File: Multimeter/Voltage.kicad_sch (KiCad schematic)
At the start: 9 parts, among them U2 LM358, U3 CD4007

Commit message: Renamed from Project1 to Multimeter
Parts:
- U3: symbol Project1:CD4007 -> Multimeter:CD4007
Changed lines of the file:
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@@
     (pin "8")
   )
-  (symbol (lib_id "Project1:CD4007") (at 158.75 78.74 0) (unit 1)
+  (symbol (lib_id "Multimeter:CD4007") (at 158.75 78.74 0) (unit 1)
     (in_bom yes) (on_board yes) (fields_autoplaced)
     (property "Reference" "U3" (id 0) (at 158.75 63.4705 0))

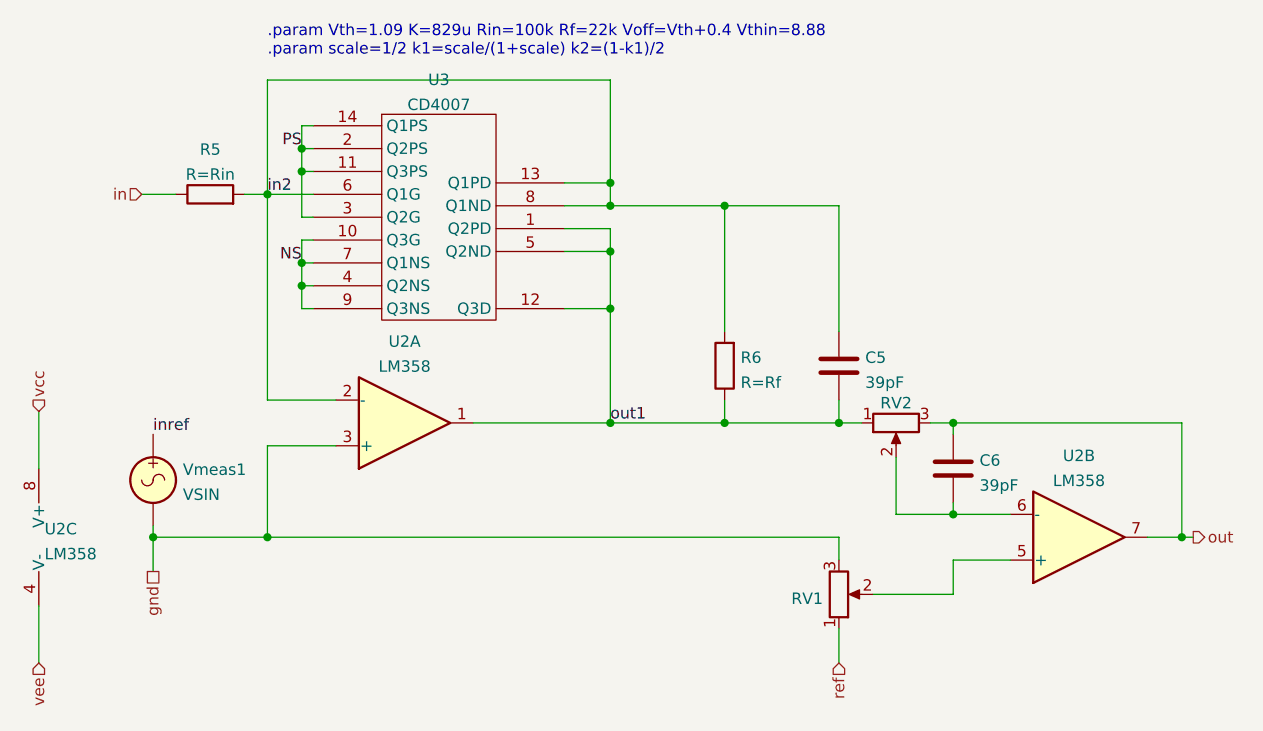
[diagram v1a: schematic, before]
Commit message: Reconnected CD4007 to use only two transistors
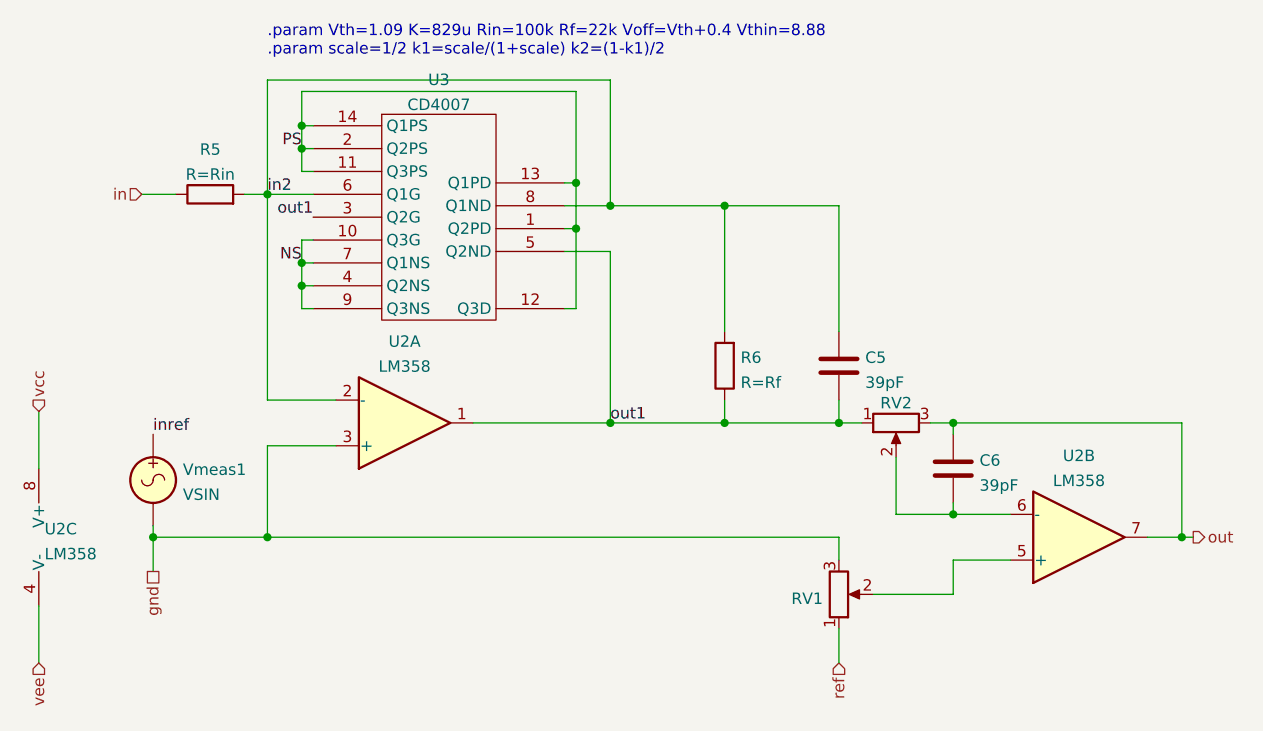
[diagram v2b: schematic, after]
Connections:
- net PS: now also U3.1 (Q2PD), U3.12 (Q3D), U3.13 (Q1PD); no longer U3.3 (Q2G)
- net in2: no longer U3.13 (Q1PD)
- net out1: now also U3.3 (Q2G); no longer U3.1 (Q2PD), U3.12 (Q3D)
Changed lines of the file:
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@@
 (kicad_sch (version 20211123) (generator eeschema)
   (paper "A4")
+  (junction (at 143.51 68.58) (diameter 0) (color 0 0 0 0)
+  )
   (junction (at 177.8 101.6) (diameter 0) (color 0 0 0 0)
   )
-  (junction (at 143.51 73.66) (diameter 0) (color 0 0 0 0)
+  (junction (at 173.99 80.01) (diameter 0) (color 0 0 0 0)
   )
   (junction (at 190.5 101.6) (diameter 0) (color 0 0 0 0)
   )
-  (junction (at 177.8 74.93) (diameter 0) (color 0 0 0 0)
-  )
   (junction (at 139.7 114.3) (diameter 0) (color 0 0 0 0)
   )
-  (junction (at 177.8 82.55) (diameter 0) (color 0 0 0 0)
-  )
-  (junction (at 177.8 88.9) (diameter 0) (color 0 0 0 0)
-  )
   (junction (at 143.51 86.36) (diameter 0) (color 0 0 0 0)
   )
@@
   (junction (at 215.9 101.6) (diameter 0) (color 0 0 0 0)
   )
+  (junction (at 143.51 83.82) (diameter 0) (color 0 0 0 0)
+  )
   (junction (at 139.7 76.2) (diameter 0) (color 0 0 0 0)
   )
@@
   (junction (at 143.51 71.12) (diameter 0) (color 0 0 0 0)
   )
-  (junction (at 143.51 83.82) (diameter 0) (color 0 0 0 0)
-  )
   (junction (at 127 114.3) (diameter 0) (color 0 0 0 0)
   )
+  (junction (at 173.99 74.93) (diameter 0) (color 0 0 0 0)
+  )
   (junction (at 203.2 101.6) (diameter 0) (color 0 0 0 0)
   )
@@
     (stroke (width 0) (type default) (color 0 0 0 0))
   )
+  (wire (pts (xy 143.51 81.28) (xy 143.51 83.82))
+    (stroke (width 0) (type default) (color 0 0 0 0))
+  )
   (wire (pts (xy 190.5 99.06) (xy 190.5 101.6))
     (stroke (width 0) (type default) (color 0 0 0 0))
@@
     (stroke (width 0) (type default) (color 0 0 0 0))
   )
-  (wire (pts (xy 177.8 74.93) (xy 177.8 77.47))
-    (stroke (width 0) (type default) (color 0 0 0 0))
-  )
   (wire (pts (xy 213.36 101.6) (xy 215.9 101.6))
     (stroke (width 0) (type default) (color 0 0 0 0))
@@
     (stroke (width 0) (type default) (color 0 0 0 0))
   )
-  (wire (pts (xy 143.51 83.82) (xy 143.51 81.28))
-    (stroke (width 0) (type default) (color 0 0 0 0))
-  )
-  (wire (pts (xy 177.8 88.9) (xy 177.8 101.6))
+  (wire (pts (xy 173.99 80.01) (xy 173.99 88.9))
     (stroke (width 0) (type default) (color 0 0 0 0))
   )
@@
     (stroke (width 0) (type default) (color 0 0 0 0))
   )
+  (wire (pts (xy 173.99 64.77) (xy 173.99 74.93))
+    (stroke (width 0) (type default) (color 0 0 0 0))
+  )
   (wire (pts (xy 127 113.03) (xy 127 114.3))
     (stroke (width 0) (type default) (color 0 0 0 0))
@@
     (stroke (width 0) (type default) (color 0 0 0 0))
   )
+  (wire (pts (xy 144.78 81.28) (xy 143.51 81.28))
+    (stroke (width 0) (type default) (color 0 0 0 0))
+  )
   (wire (pts (xy 203.2 101.6) (xy 190.5 101.6))
     (stroke (width 0) (type default) (color 0 0 0 0))
@@
     (stroke (width 0) (type default) (color 0 0 0 0))
   )
-  (wire (pts (xy 172.72 88.9) (xy 177.8 88.9))
+  (wire (pts (xy 172.72 88.9) (xy 173.99 88.9))
     (stroke (width 0) (type default) (color 0 0 0 0))
   )
@@
   )
   (wire (pts (xy 139.7 114.3) (xy 127 114.3))
+    (stroke (width 0) (type default) (color 0 0 0 0))
+  )
+  (wire (pts (xy 143.51 68.58) (xy 143.51 64.77))
     (stroke (width 0) (type default) (color 0 0 0 0))
   )
@@
     (stroke (width 0) (type solid) (color 0 0 0 0))
   )
-  (wire (pts (xy 172.72 80.01) (xy 177.8 80.01))
-    (stroke (width 0) (type default) (color 0 0 0 0))
-  )
   (wire (pts (xy 144.78 73.66) (xy 143.51 73.66))
     (stroke (width 0) (type default) (color 0 0 0 0))
   )
-  (wire (pts (xy 143.51 81.28) (xy 144.78 81.28))
-    (stroke (width 0) (type default) (color 0 0 0 0))
-  )
   (wire (pts (xy 209.55 111.76) (xy 215.9 111.76))
     (stroke (width 0) (type default) (color 0 0 0 0))
   )
-  (wire (pts (xy 143.51 78.74) (xy 143.51 73.66))
+  (wire (pts (xy 173.99 80.01) (xy 172.72 80.01))
     (stroke (width 0) (type default) (color 0 0 0 0))
   )
@@
     (stroke (width 0) (type default) (color 0 0 0 0))
   )
-  (wire (pts (xy 177.8 74.93) (xy 172.72 74.93))
-    (stroke (width 0) (type default) (color 0 0 0 0))
-  )
   (wire (pts (xy 215.9 101.6) (xy 241.3 101.6))
     (stroke (width 0) (type default) (color 0 0 0 0))
@@
     (stroke (width 0) (type default) (color 0 0 0 0))
   )
-  (wire (pts (xy 144.78 78.74) (xy 143.51 78.74))
+  (wire (pts (xy 173.99 74.93) (xy 173.99 80.01))
     (stroke (width 0) (type default) (color 0 0 0 0))
   )
@@
     (stroke (width 0) (type default) (color 0 0 0 0))
   )
-  (wire (pts (xy 177.8 82.55) (xy 177.8 88.9))
+  (wire (pts (xy 177.8 82.55) (xy 177.8 101.6))
+    (stroke (width 0) (type default) (color 0 0 0 0))
+  )
+  (wire (pts (xy 143.51 64.77) (xy 173.99 64.77))
     (stroke (width 0) (type default) (color 0 0 0 0))
   )
@@
     (stroke (width 0) (type default) (color 0 0 0 0))
   )
-  (wire (pts (xy 177.8 63.5) (xy 177.8 74.93))
+  (wire (pts (xy 177.8 63.5) (xy 177.8 77.47))
     (stroke (width 0) (type default) (color 0 0 0 0))
   )
@@
     (stroke (width 0) (type default) (color 0 0 0 0))
   )
+  (wire (pts (xy 172.72 74.93) (xy 173.99 74.93))
+    (stroke (width 0) (type default) (color 0 0 0 0))
+  )
   (wire (pts (xy 139.7 104.14) (xy 139.7 114.3))
     (stroke (width 0) (type default) (color 0 0 0 0))
   )
   (wire (pts (xy 139.7 63.5) (xy 177.8 63.5))
-    (stroke (width 0) (type default) (color 0 0 0 0))
-  )
-  (wire (pts (xy 177.8 80.01) (xy 177.8 82.55))
     (stroke (width 0) (type default) (color 0 0 0 0))
   )
@@
     (effects (font (size 1.27 1.27)) (justify right bottom))
   )
+  (label "out1" (at 144.78 78.74 180)
+    (effects (font (size 1.27 1.27)) (justify right bottom))
+  )
